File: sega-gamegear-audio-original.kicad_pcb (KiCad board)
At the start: 2 copper layers, 20 parts, among them CN1 CONN 2P, CN2 292161-6, IC1 TDA2822D, J1 PJ-307A

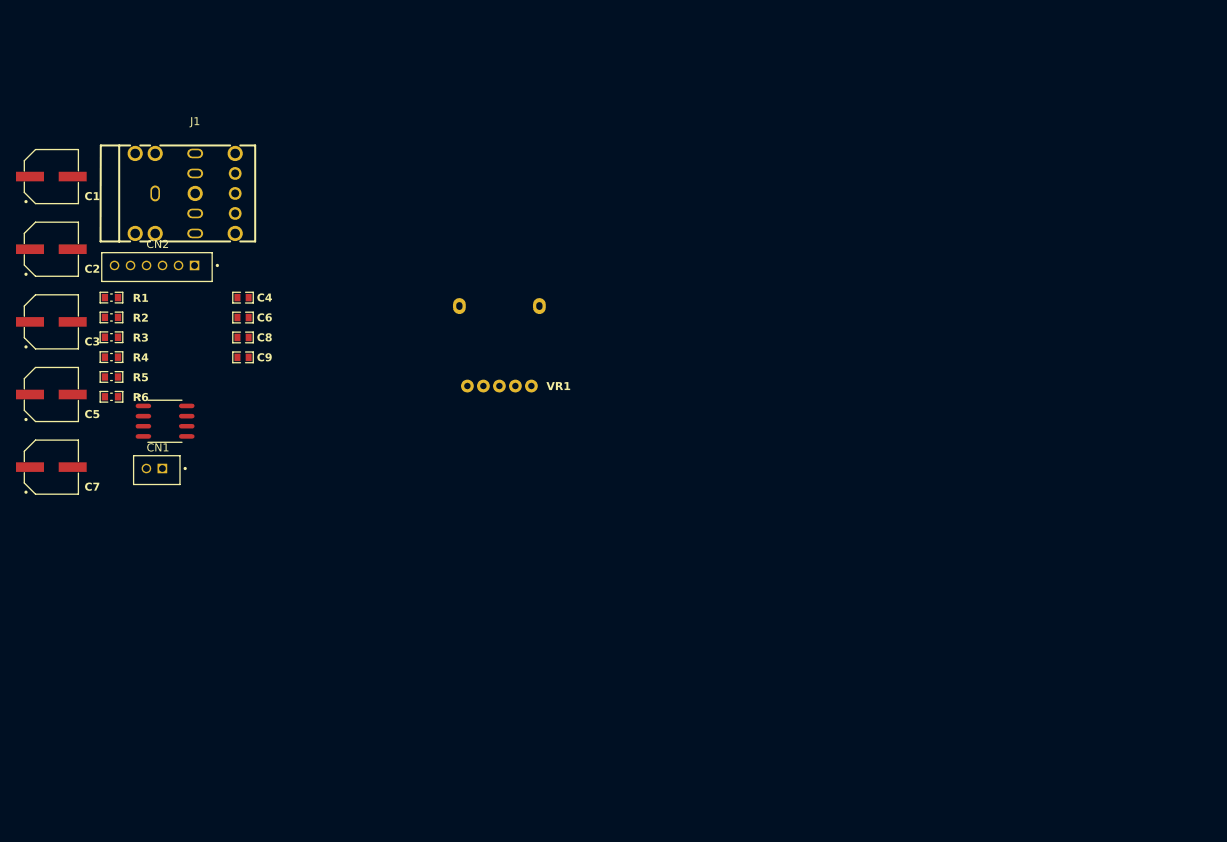
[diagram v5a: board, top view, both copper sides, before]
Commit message: add board outline
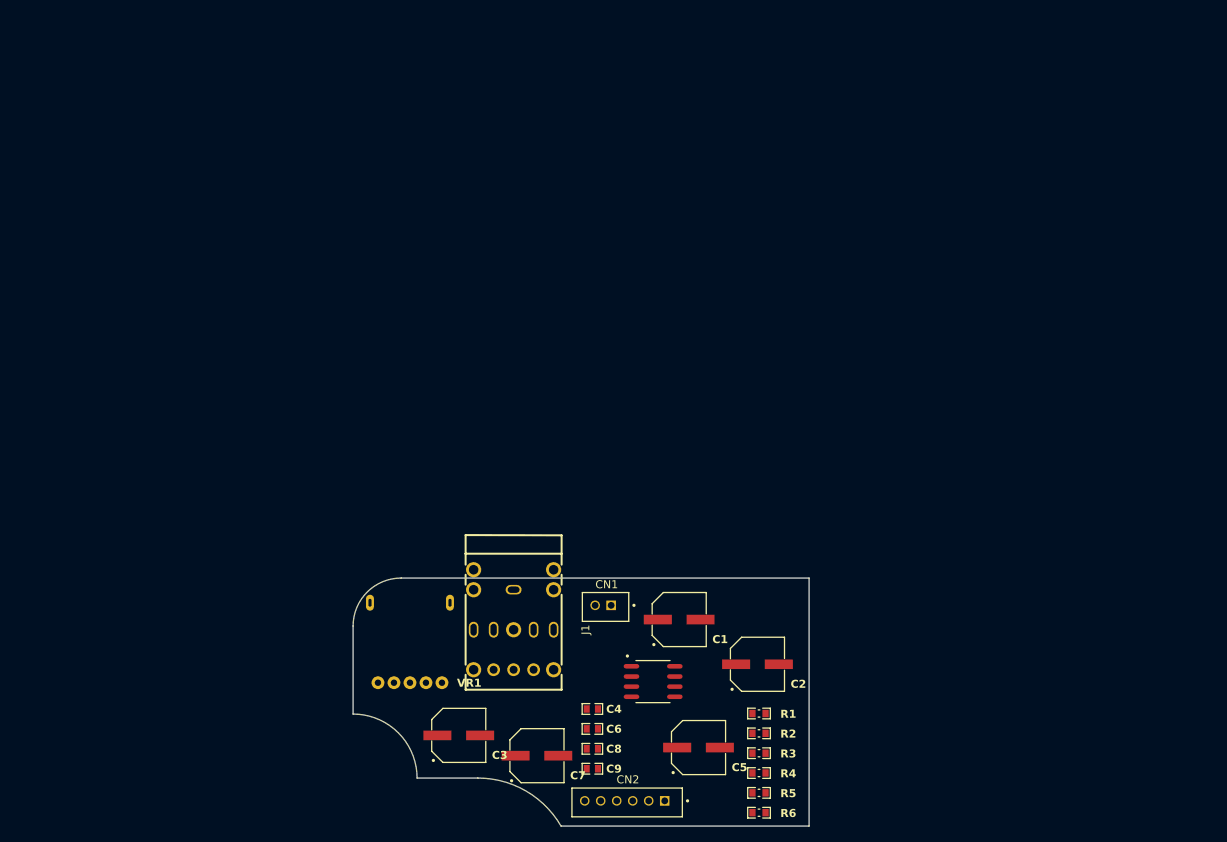
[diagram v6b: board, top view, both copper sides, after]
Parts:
- IC1: value TDA2822D -> Val**
- moved C2 102.4 mm to (173.2, 96.0)
- moved R1 96.2 mm to (173.4, 102.2)
- moved R2 96.2 mm to (173.4, 104.6)
- moved R3 96.2 mm to (173.4, 107.1)
- moved R4 96.2 mm to (173.4, 109.6)
- moved R5 96.2 mm to (173.4, 112.1)
- moved R6 96.2 mm to (173.4, 114.6)
- moved C1 96.0 mm to (163.4, 90.4)
- moved C5 92.2 mm to (165.9, 106.4)
- moved CN2 89.1 mm to (161.6, 113.1)
- moved C3 72.6 mm to (135.9, 104.9)
- moved C7 70.6 mm to (145.7, 107.4)
- moved IC1 69.1 mm to (160.2, 98.2)
- moved J1 67.5 mm to (142.7, 91.7), turned to -90 degrees
- moved C6 67.5 mm to (152.6, 104.1)
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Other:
- board outline added: 57 x 31 mm

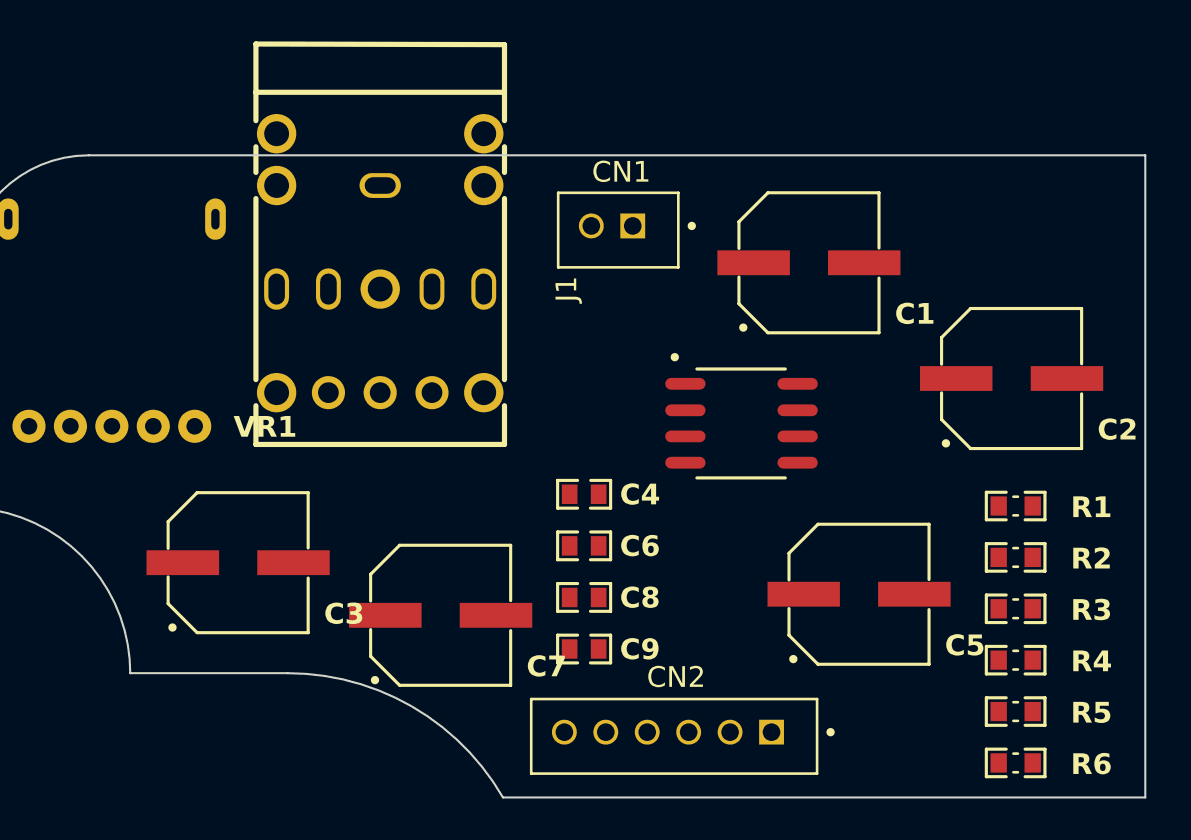
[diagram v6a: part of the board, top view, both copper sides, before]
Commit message: add board settings for jlcpcb
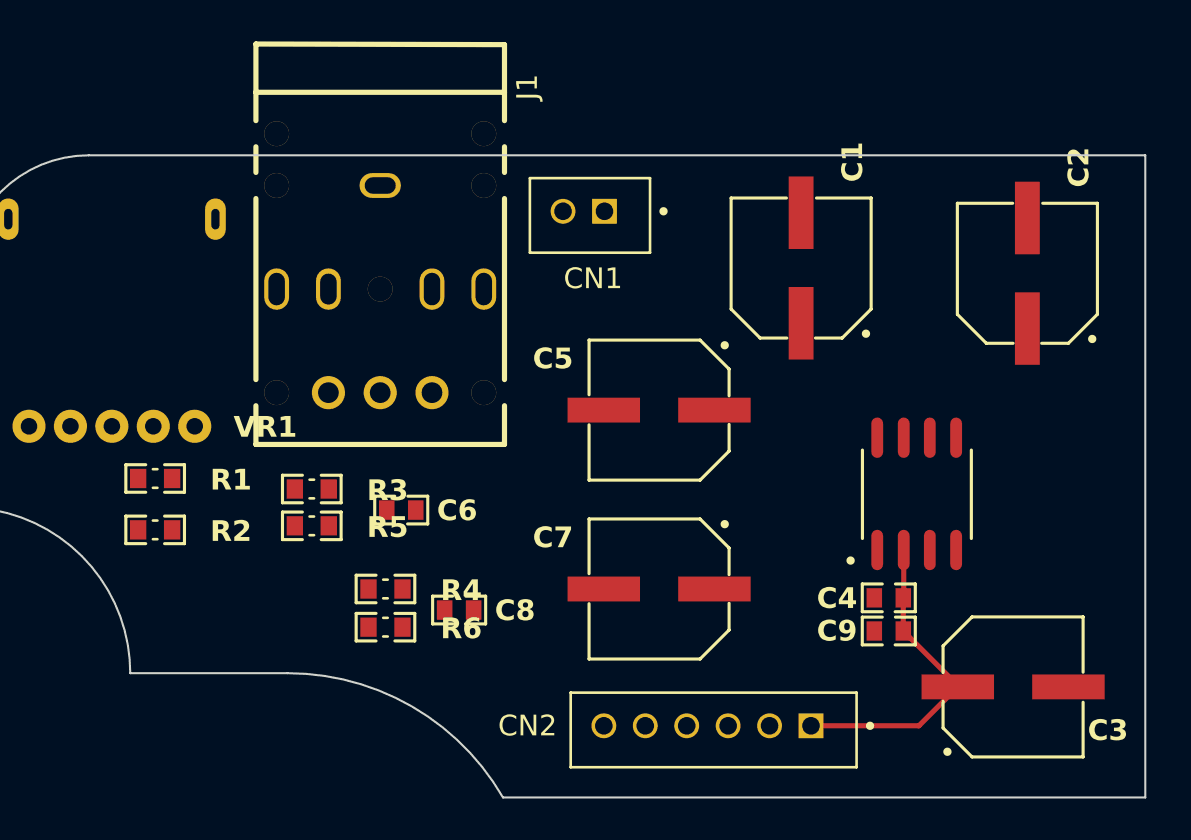
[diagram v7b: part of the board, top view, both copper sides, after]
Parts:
- J1: value PJ-307A -> PJ-307
- moved R1 41.6 mm to (131.9, 100.8)
- moved R2 41.6 mm to (131.9, 103.3)
- moved C3 37.9 mm to (173.3, 110.9)
- moved R5 35.1 mm to (139.4, 103.1)
- moved R3 34.5 mm to (139.4, 101.3)
- moved R6 31.1 mm to (143.0, 108.0)
- moved R4 30.6 mm to (143.0, 106.2)
- moved C4 15.5 mm to (167.3, 106.6)
- moved C9 14.7 mm to (167.3, 108.2)
- moved C5 13.1 mm to (156.2, 97.5), turned to 180 degrees
- moved C7 10.6 mm to (156.2, 106.2), turned to 180 degrees
- moved IC1 9.15 mm to (168.7, 101.6), turned to 90 degrees
- moved C6 9.00 mm to (143.8, 102.4)
- moved C8 6.06 mm to (146.6, 107.2)
- moved C2 5.14 mm to (174.0, 90.9), turned to 90 degrees
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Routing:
- net Net-(CN2-5V): track 0.00 -> 15.6 mm

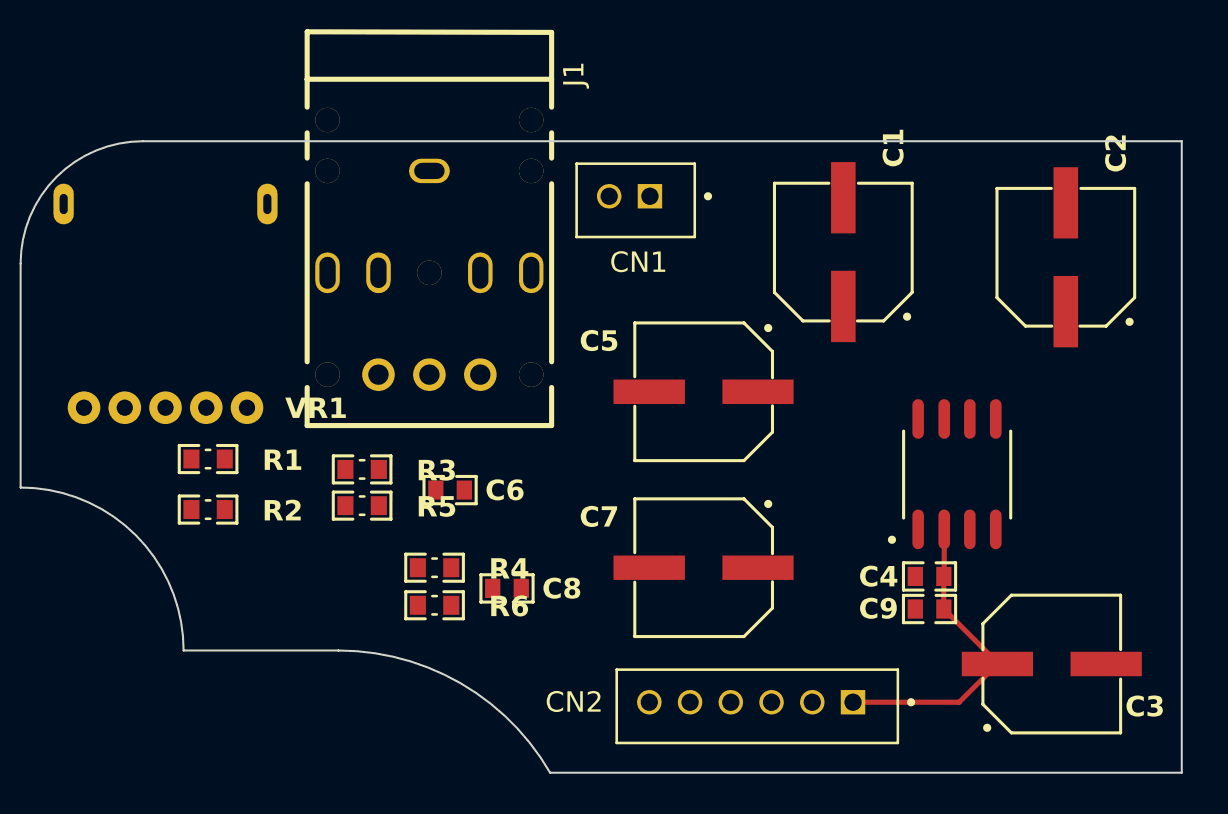
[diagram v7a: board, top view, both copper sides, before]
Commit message: slightly better potentiometer 3d file
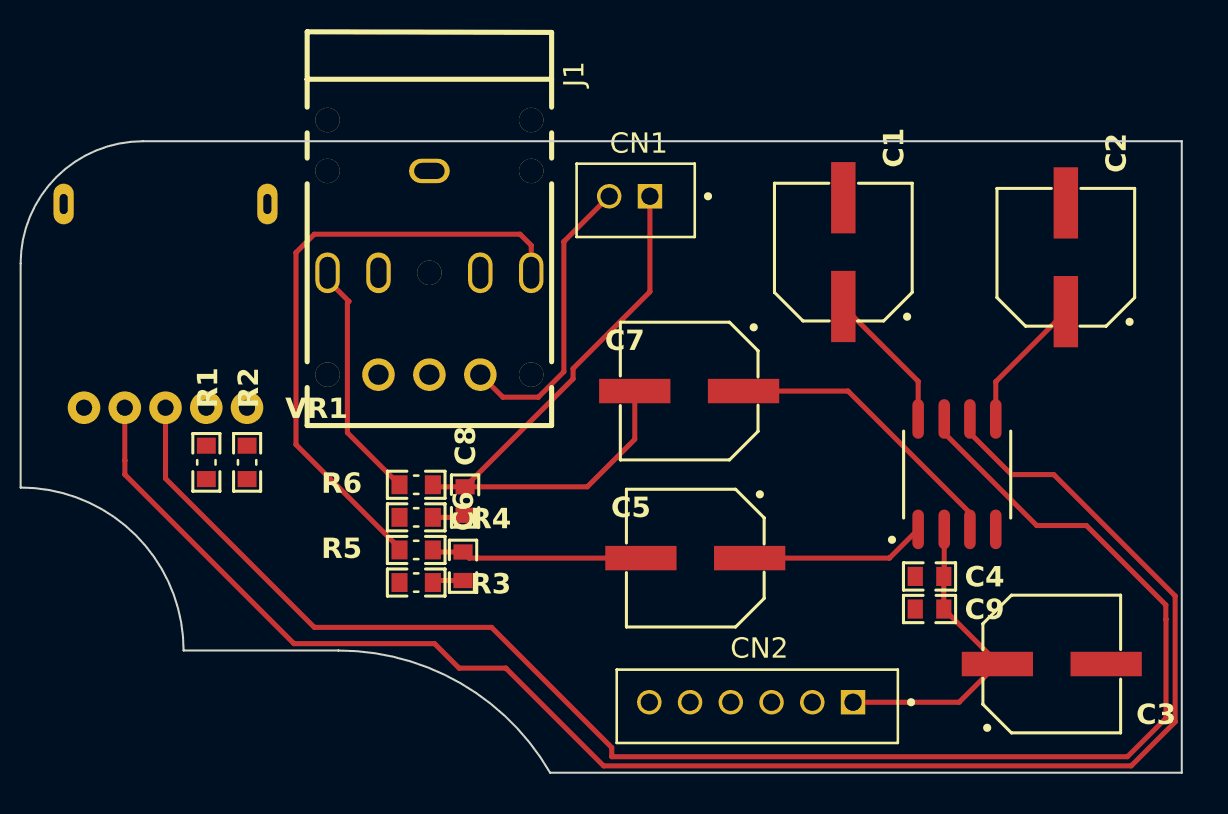
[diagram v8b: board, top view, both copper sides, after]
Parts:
- J1: value PJ-307 -> CONN MINI JACK
- moved C7 8.70 mm to (155.5, 97.5)
- moved C5 8.17 mm to (155.8, 105.7)
- moved R3 6.16 mm to (142.1, 106.9)
- moved R6 5.98 mm to (142.1, 102.1), turned to 180 degrees
- moved C8 4.76 mm to (144.5, 102.9), turned to 90 degrees
- moved C6 3.79 mm to (144.4, 106.1), turned to 90 degrees
- moved R5 3.43 mm to (142.1, 105.3), turned to 180 degrees
- moved R2 3.01 mm to (133.8, 101.0), turned to 90 degrees
- moved R4 2.63 mm to (142.1, 103.7)
- moved R1 0.18 mm to (131.8, 101.0), turned to 90 degrees
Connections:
- C1 pad 1: Net-(IC1--I2) -> Net-(IC1--I1)
- C2 pad 1: Net-(C2-Pad1) -> Net-(IC1--I2)
- IC1 pad 6: Net-(IC1-+I2-Pad6) -> Net-(IC1-+I2)
- IC1 pad 8: Net-(C2-Pad1) -> Net-(IC1--I1)
- VR1 pad 1: Net-(R1-Pad2) -> GND
- VR1 pad 2: Net-(IC1-+I1) -> Net-(IC1-+I2)
- VR1 pad 3: Net-(R2-Pad2) -> Net-(IC1-+I1)
- VR1 pad 4: Net-(IC1-+I2-Pad6) -> Net-(R1-Pad2)
- VR1 pad 5: GND -> Net-(R2-Pad2)
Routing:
- net Net-(IC1-+I2): track 0.00 -> 81.9 mm
- net Net-(IC1-+I1): track 0.00 -> 79.9 mm
- net Net-(CN1-SP+): track 0.00 -> 31.3 mm
- net Net-(J1-Pad3): track 0.00 -> 30.2 mm
- net Net-(CN1-SP-): track 0.00 -> 14.6 mm
- net Net-(IC1-02): track 0.00 -> 14.4 mm
- net Net-(J1-Pad2): track 0.00 -> 11.9 mm
- net Net-(C5-Pad2): track 0.00 -> 10.4 mm
- net Net-(IC1-O1): track 0.00 -> 8.86 mm
- net Net-(IC1--I1): track 0.00 -> 7.04 mm
- net Net-(IC1--I2): track 0.00 -> 6.69 mm
- net Net-(C8-Pad1): track 0.00 -> 1.62 mm
- net Net-(C6-Pad1): track 0.00 -> 1.52 mm
